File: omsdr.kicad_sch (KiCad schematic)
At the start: 54 parts, among them J1 I/Q Out, J2 ANT, J3 ISP, J4 LO, J5 I/Q Out, J8 PWR, SW1 SW_SPST, SW2 SW_SPST, T1 CX2074NL, U1 LT6231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

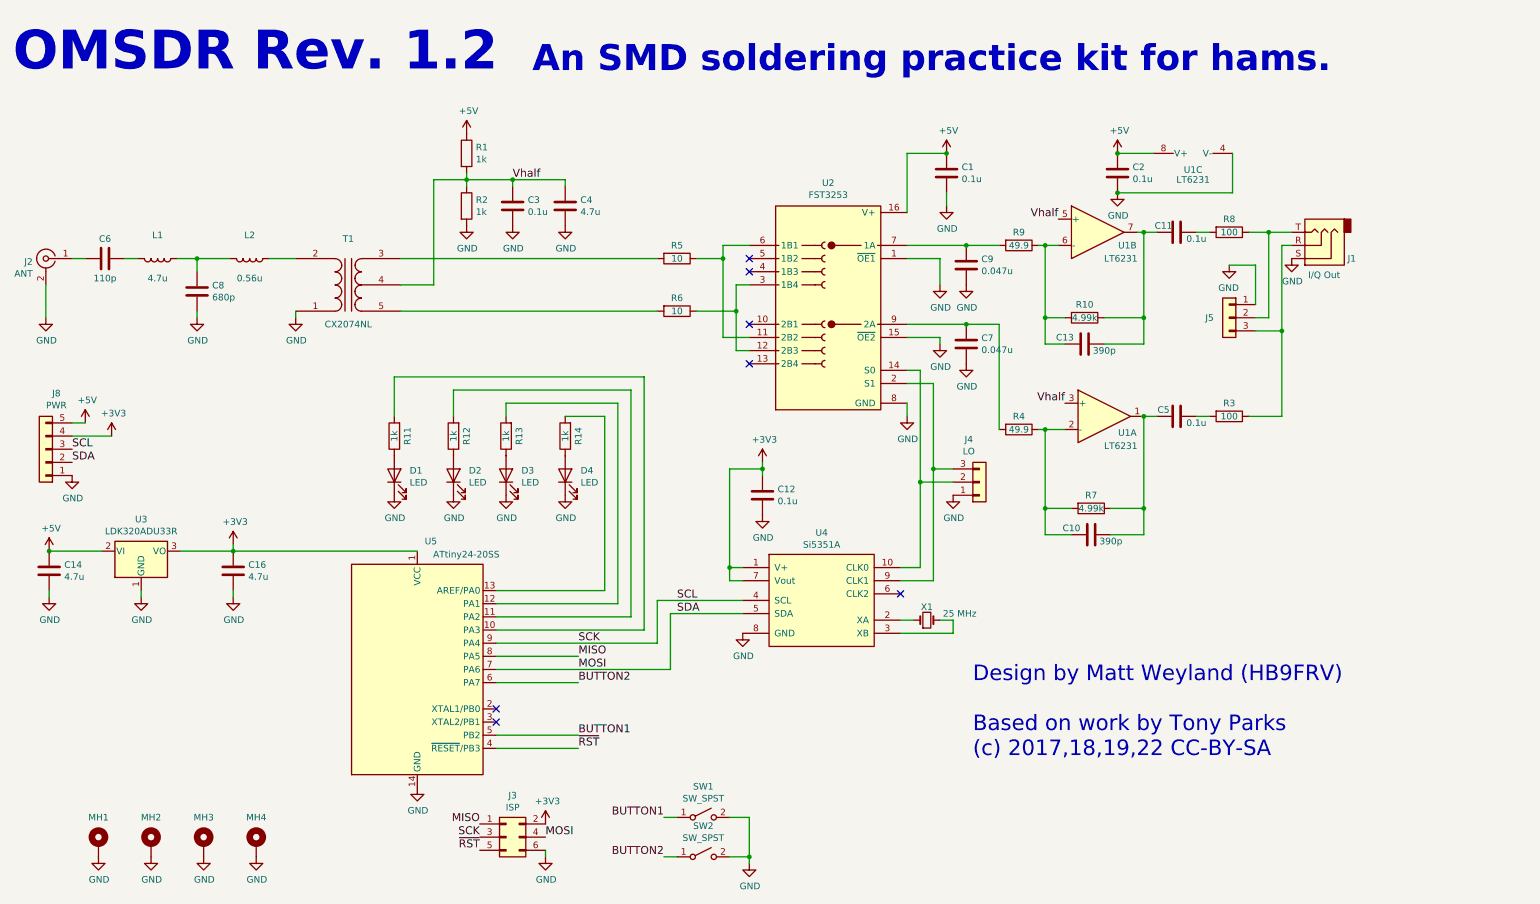
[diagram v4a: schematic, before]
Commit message: Using Si5351 from the KiCad library (sch & pcb)
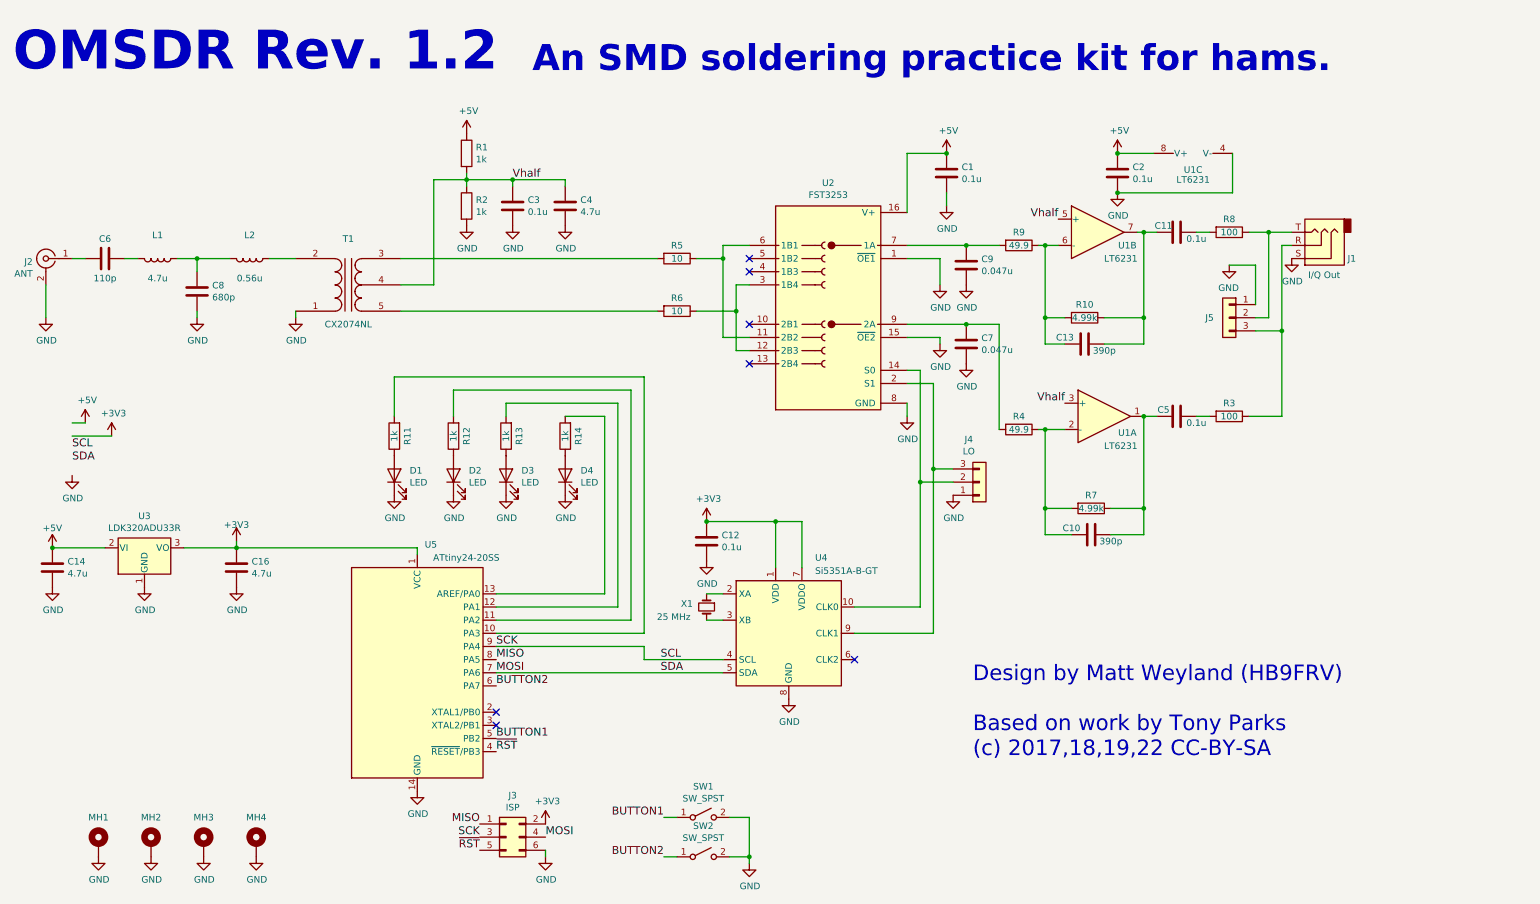
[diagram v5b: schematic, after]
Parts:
- removed J8: PWR, Connector_PinHeader_2.54mm:PinHeader_1x05_P2.54mm_Horizontal, symbol Connector_Generic:Conn_01x05
- removed U4: Si5351A, IPC7351-Most:SOP50P490X110-10, symbol silabs:Si5351A
- added U4: Si5351A-B-GT, Package_SO:MSOP-10_3x3mm_P0.5mm, symbol Oscillator:Si5351A-B-GT
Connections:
- net +3V3: now also U4.1 (VDD), U4.7 (VDDO)
- net GND: now also U4.8 (GND)
- net MOSI: now also U4.5 (SDA)
- net SCK: now also U4.4 (SCL)
- net at J4.2 (Pin_2), U2.14 (S0): now also U4.10 (CLK0)
- net at J4.3 (Pin_3), U2.2 (S1): now also U4.9 (CLK1)
- net at X1.1: now also U4.2 (XA)
- net at X1.2: now also U4.3 (XB)
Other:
- moved on the sheet: C12, C14, C16, U3, U5, X1

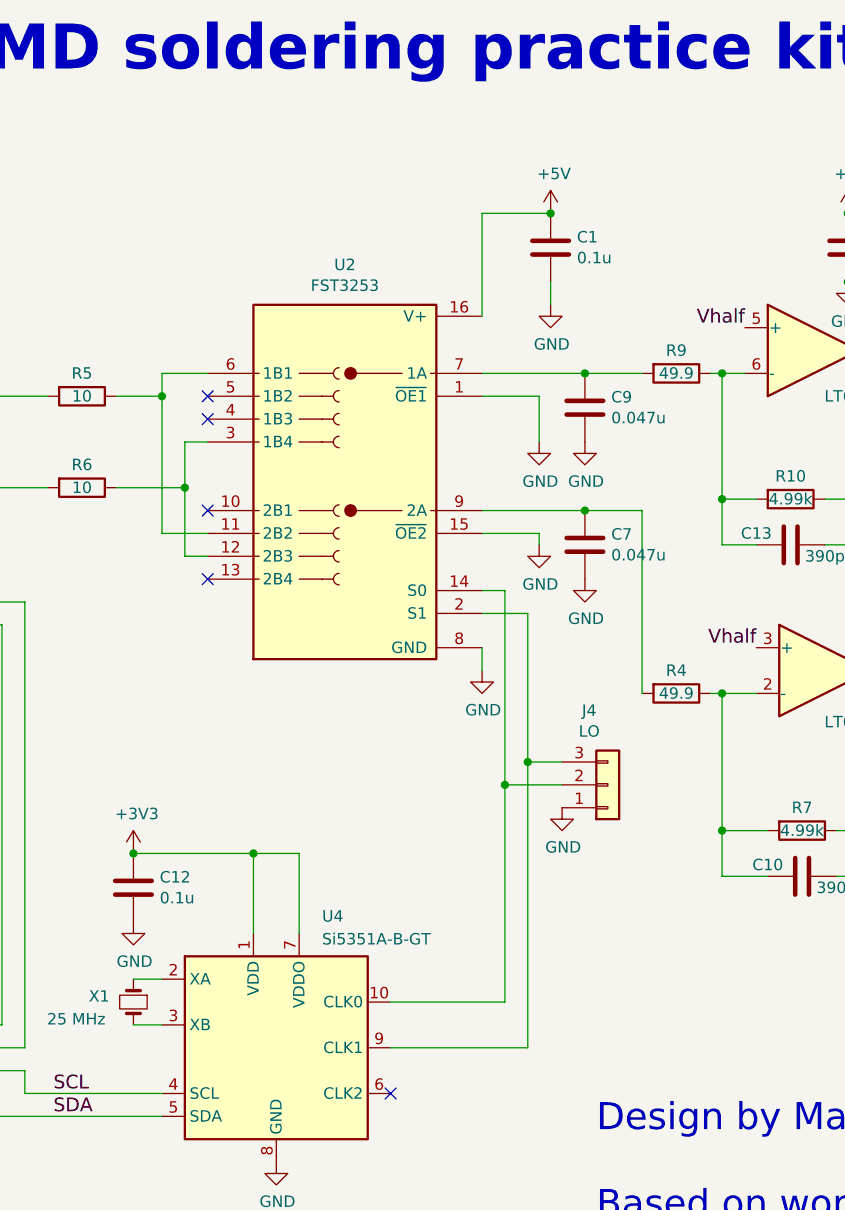
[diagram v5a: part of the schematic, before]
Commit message: Using FST3253 from the KiCad library (sch & pcb)
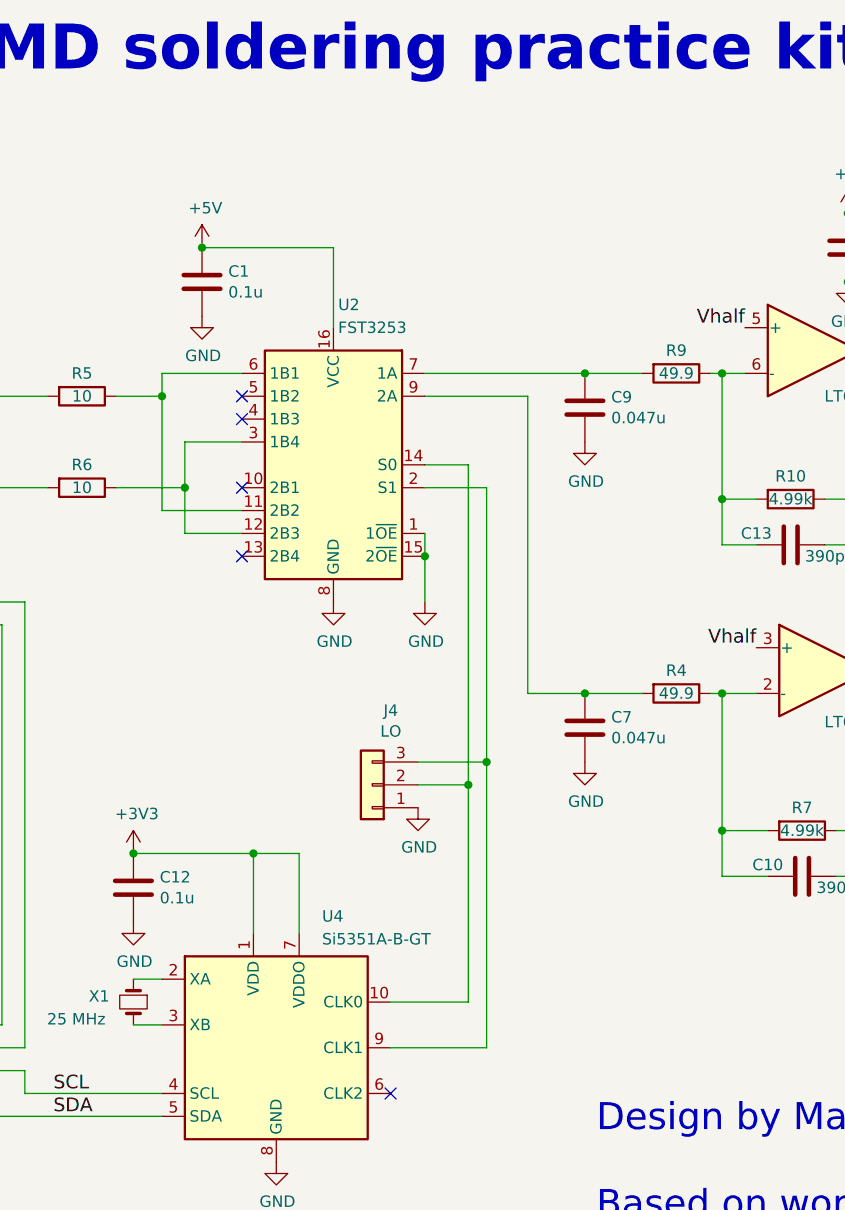
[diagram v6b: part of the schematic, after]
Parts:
- removed U2: FST3253, IPC7351-Most:SOIC127P600X180-16, symbol onsemi:FST3253
- added U2: FST3253, Package_SO:SOIC-16_3.9x9.9mm_P1.27mm, symbol Analog_Switch:SN74CBT3253
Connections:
- net +5V: now also U2.16 (VCC)
- net GND: now also U2.1 (1~{OE}), U2.15 (2~{OE}), U2.8 (GND)
- net at R5.1: now also U2.11 (2B2), U2.6 (1B1)
- net at R6.1: now also U2.12 (2B3), U2.3 (1B4)
- net at J4.2 (Pin_2), U4.10 (CLK0): now also U2.14 (S0)
- net at J4.3 (Pin_3), U4.9 (CLK1): now also U2.2 (S1)
- net at C9.1, R9.2: now also U2.7 (1A)
- net at C7.1, R4.2: now also U2.9 (2A)
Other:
- moved on the sheet: C1, C7, J4

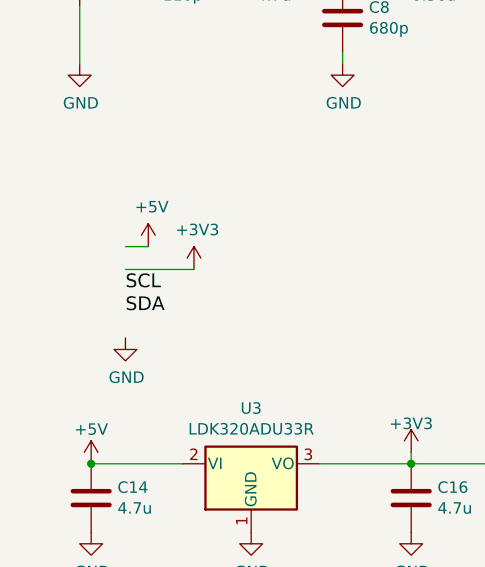
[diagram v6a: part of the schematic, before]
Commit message: Replacing some passives with current kicad symbols/footprints
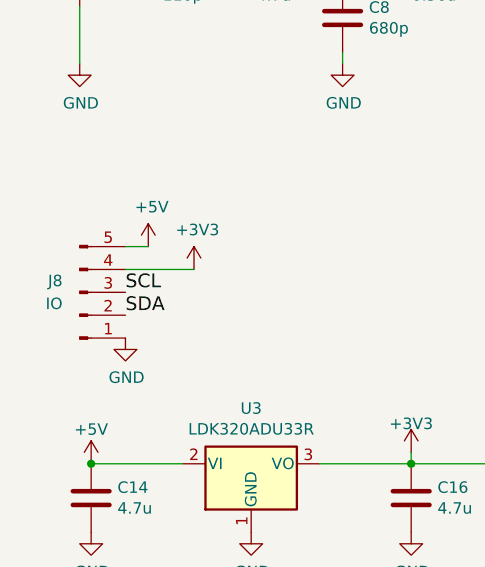
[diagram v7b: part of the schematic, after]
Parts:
- added J8: IO, Connector_PinHeader_2.54mm:PinHeader_1x05_P2.54mm_Horizontal, symbol Connector:Conn_01x05_Male
- C1, C10, C11, C12, C13, C14, C16, C2, C3, C4, C5, C6, C7, C8, C9: footprint Capacitor_SMD:C_1206_3216Metric_Pad1.42x1.75mm_HandSolder -> Capacitor_SMD:C_1206_3216Metric_Pad1.33x1.80mm_HandSolder
- J2: footprint local:SMA_edge_mount_small -> Connector_Coaxial:SMA_Samtec_SMA-J-P-X-ST-EM1_EdgeMount
- R1, R10, R11, R12, R13, R14, R2, R3, R4, R5, R6, R7, R8, R9: footprint Resistor_SMD:R_1206_3216Metric_Pad1.42x1.75mm_HandSolder -> Resistor_SMD:R_1206_3216Metric_Pad1.30x1.75mm_HandSolder
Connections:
- net +3V3: now also J8.4 (Pin_4)
- net +5V: now also J8.5 (Pin_5)
- net GND: now also J8.1 (Pin_1)
- net MOSI: now also J8.2 (Pin_2)
- net SCK: now also J8.3 (Pin_3)

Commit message: Using M3 mouting holes from the KiCad library (sch & pcb)
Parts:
- MH1, MH2, MH3, MH4: footprint mech:PTH-3MM-PLUS-SUPPORTED -> MountingHole:MountingHole_3.2mm_M3_Pad_Via
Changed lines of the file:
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@@
       (effects (font (size 1.27 1.27)) (justify right))
     )
-    (property "Footprint" "mech:PTH-3MM-PLUS-SUPPORTED" (id 2) (at 35.56 175.26 0)
+    (property "Footprint" "MountingHole:MountingHole_3.2mm_M3_Pad_Via" (id 2) (at 35.56 175.26 0)
       (effects (font (size 1.27 1.27)) hide)
     )
@@
       (effects (font (size 1.27 1.27)) (justify right))
     )
-    (property "Footprint" "mech:PTH-3MM-PLUS-SUPPORTED" (id 2) (at 45.72 175.26 0)
+    (property "Footprint" "MountingHole:MountingHole_3.2mm_M3_Pad_Via" (id 2) (at 45.72 175.26 0)
       (effects (font (size 1.27 1.27)) hide)
     )
@@
       (effects (font (size 1.27 1.27)) (justify right))
     )
-    (property "Footprint" "mech:PTH-3MM-PLUS-SUPPORTED" (id 2) (at 55.88 175.26 0)
+    (property "Footprint" "MountingHole:MountingHole_3.2mm_M3_Pad_Via" (id 2) (at 55.88 175.26 0)
       (effects (font (size 1.27 1.27)) hide)
     )
@@
       (effects (font (size 1.27 1.27)) (justify right))
     )
-    (property "Footprint" "mech:PTH-3MM-PLUS-SUPPORTED" (id 2) (at 66.04 175.26 0)
+    (property "Footprint" "MountingHole:MountingHole_3.2mm_M3_Pad_Via" (id 2) (at 66.04 175.26 0)
       (effects (font (size 1.27 1.27)) hide)
     )
@@
     )
     (path "/00000000-0000-0000-0000-00005a0577ba"
-      (reference "MH1") (unit 1) (value " ") (footprint "mech:PTH-3MM-PLUS-SUPPORTED")
+      (reference "MH1") (unit 1) (value " ") (footprint "MountingHole:MountingHole_3.2mm_M3_Pad_Via")
     )
     (path "/00000000-0000-0000-0000-00005a057fc9"
-      (reference "MH2") (unit 1) (value " ") (footprint "mech:PTH-3MM-PLUS-SUPPORTED")
+      (reference "MH2") (unit 1) (value " ") (footprint "MountingHole:MountingHole_3.2mm_M3_Pad_Via")
     )
     (path "/00000000-0000-0000-0000-00005a0580bb"
-      (reference "MH3") (unit 1) (value " ") (footprint "mech:PTH-3MM-PLUS-SUPPORTED")
+      (reference "MH3") (unit 1) (value " ") (footprint "MountingHole:MountingHole_3.2mm_M3_Pad_Via")
     )
     (path "/00000000-0000-0000-0000-00005a0580c1"
-      (reference "MH4") (unit 1) (value " ") (footprint "mech:PTH-3MM-PLUS-SUPPORTED")
+      (reference "MH4") (unit 1) (value " ") (footprint "MountingHole:MountingHole_3.2mm_M3_Pad_Via")
     )
     (path "/00000000-0000-0000-0000-00005a04a538"
